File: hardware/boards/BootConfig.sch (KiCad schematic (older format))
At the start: 6 parts, among them SW1 SW_DIP_x03, U1 ECP5UM5G-381caBGA, U5 128MiB

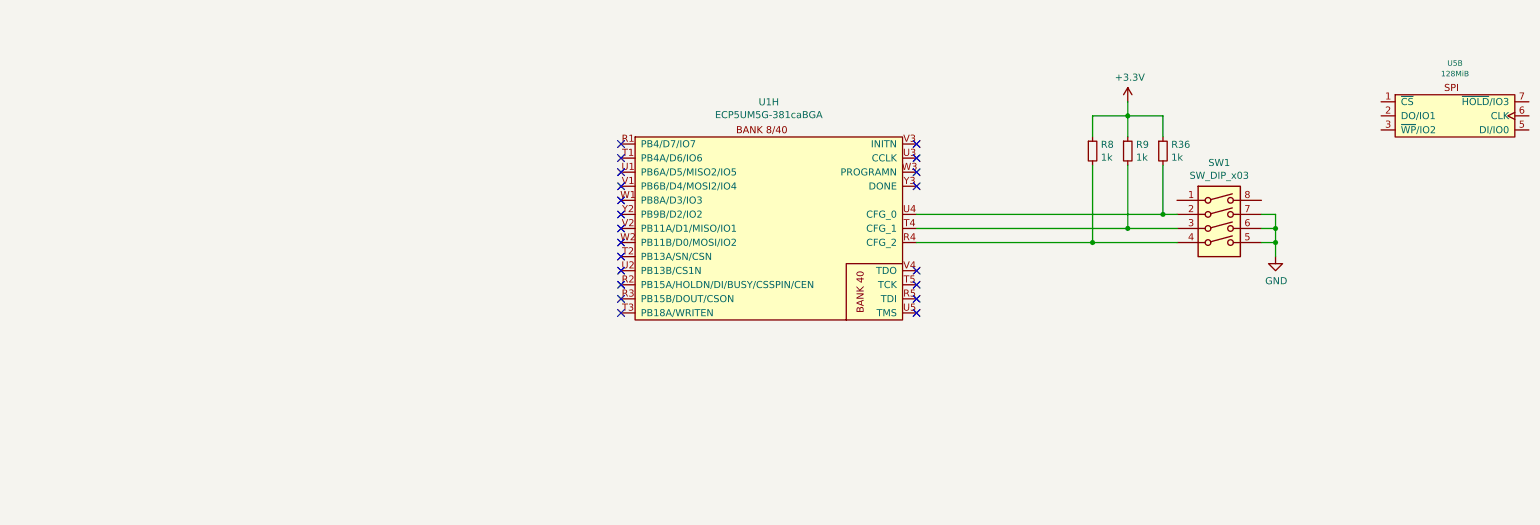
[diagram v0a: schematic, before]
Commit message: Added the JTAG header and some misc cleanup
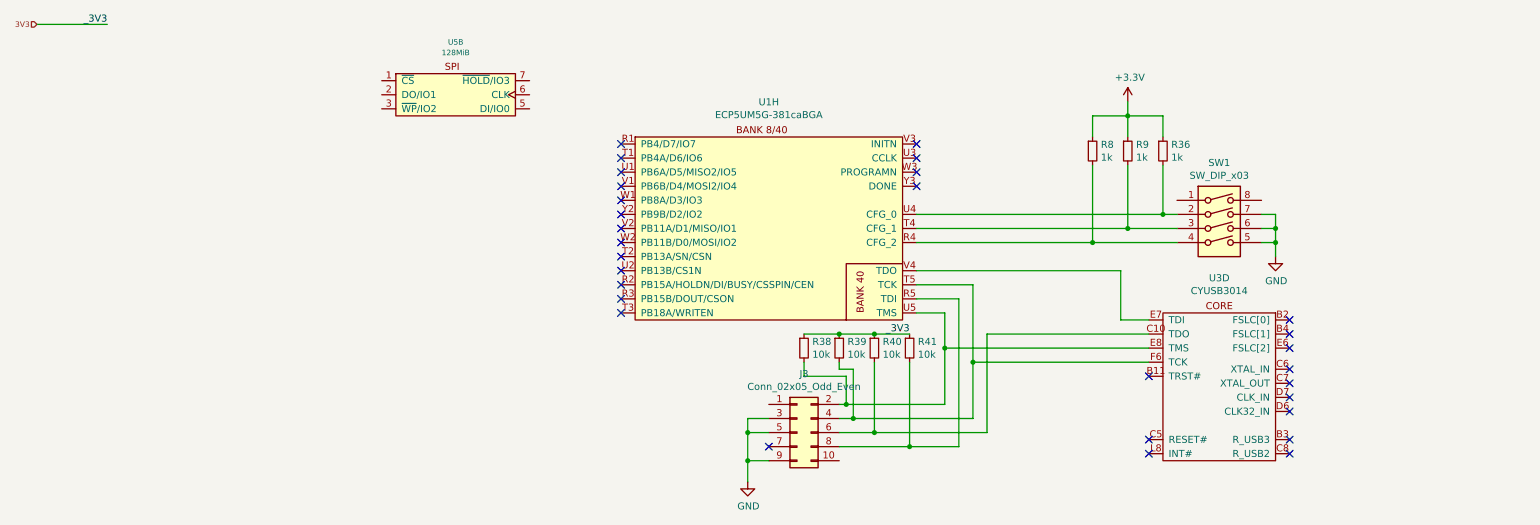
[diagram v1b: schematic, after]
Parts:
- added J3: Conn_02x05_Odd_Even, lethalbit-connectors:FTSH-105-01-L-DV-K-TR, symbol Connector_Generic:Conn_02x05_Odd_Even
- added R38, R39, R40, R41: 10k, Resistor_SMD:R_0603_1608Metric, symbol Device:R_Small
- added U3: CYUSB3014, lethalbit:BGA-121_11x11_10.0x10.0mm, symbol lethalbit:CYUSB3014
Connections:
- net GND: now also J3.3 (Pin_3), J3.5 (Pin_5), J3.9 (Pin_9)
- net at U1.R5 (TDI): now also J3.8 (Pin_8), R41.2
- net at U1.T5 (TCK): now also J3.4 (Pin_4), R39.2, U3.F6 (TCK)
- net at U1.U5 (TMS): now also J3.2 (Pin_2), R38.2, U3.E8 (TMS)
- net at U1.V4 (TDO): now also U3.E7 (TDI)
- new net: J3.6 (Pin_6), R40.2, U3.C10 (TDO)
- new net 3V3: R38.1, R39.1, R40.1, R41.1
- no-connect marks 21 -> 30
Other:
- moved on the sheet: U5B
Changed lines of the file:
@@
 NoConn ~ 4900 2550
 NoConn ~ 4900 2650
-NoConn ~ 7000 2650
-NoConn ~ 7000 2550
-NoConn ~ 7000 2450
-NoConn ~ 7000 2350
 NoConn ~ 7000 1750
 NoConn ~ 7000 1650
@@
 L lethalbit-memory:W25N01GVZEIG U5
 U 2 1 5F1F6855
-P 10800 1100
-F 0 "U5" H 10825 1324 39  0000 C CNN
-F 1 "128MiB" H 10825 1249 39  0000 C CNN
-F 2 "lethalbit-memory:WSON-8-1EP-6.0x8.0mm" H 10800 1250 39  0001 C CNN
-F 3 "https://www.winbond.com/resource-files/w25n01gv%20revl%20050918%20unsecured.pdf" H 10800 1250 39  0001 C CNN
-F 4 "Winbond" H 10800 1100 50  0001 C CNN "MFR"
-F 5 "W25N01GVZEIG TR" H 10800 1100 50  0001 C CNN "MPN"
-	2    10800 1100
-	1    0    0    -1
-$EndComp
+P 3700 950
+F 0 "U5" H 3725 1174 39  0000 C CNN
+F 1 "128MiB" H 3725 1099 39  0000 C CNN
+F 2 "lethalbit-memory:WSON-8-1EP-6.0x8.0mm" H 3700 1100 39  0001 C CNN
+F 3 "https://www.winbond.com/resource-files/w25n01gv%20revl%20050918%20unsecured.pdf" H 3700 1100 39  0001 C CNN
+F 4 "Winbond" H 3700 950 50  0001 C CNN "MFR"
+F 5 "W25N01GVZEIG TR" H 3700 950 50  0001 C CNN "MPN"
+	2    3700 950
+	1    0    0    -1
+$EndComp
+$Comp
+L Connector_Generic:Conn_02x05_Odd_Even J3
+U 1 1 5FC2DE7F
+P 6150 3500
+F 0 "J3" H 6200 3917 50  0000 C CNN
+F 1 "Conn_02x05_Odd_Even" H 6200 3826 50  0000 C CNN
+F 2 "lethalbit-connectors:FTSH-105-01-L-DV-K-TR" H 6150 3500 50  0001 C CNN
+F 3 "~" H 6150 3500 50  0001 C CNN
+F 4 "Samtec" H 6150 3500 50  0001 C CNN "MFR"
+F 5 "FTSH-105-01-L-DV-K-TR" H 6150 3500 50  0001 C CNN "MPN"
+	1    6150 3500
+	1    0    0    -1
+$EndComp
+NoConn ~ 5950 3600
+$Comp
+L power:GND #PWR0127
+U 1 1 5FC38CCB
+P 5800 3850
+F 0 "#PWR0127" H 5800 3600 50  0001 C CNN
+F 1 "GND" H 5805 3677 50  0000 C CNN
+F 2 "" H 5800 3850 50  0001 C CNN
+F 3 "" H 5800 3850 50  0001 C CNN
+	1    5800 3850
+	1    0    0    -1
+$EndComp
+Wire Wire Line
+	5800 3850 5800 3700
+Wire Wire Line
+	5800 3400 5950 3400
+Wire Wire Line
+	5950 3500 5800 3500
+Connection ~ 5800 3500
+Wire Wire Line
+	5800 3500 5800 3400
+Wire Wire Line
+	5950 3700 5800 3700
+Connection ~ 5800 3700
+Wire Wire Line
+	5800 3700 5800 3500
+NoConn ~ 9650 2700
+NoConn ~ 9650 2800
+NoConn ~ 9650 2900
+NoConn ~ 9650 3050
+NoConn ~ 9650 3150
+NoConn ~ 9650 3250
+NoConn ~ 9650 3350
+NoConn ~ 9650 3550
+NoConn ~ 9650 3650
+NoConn ~ 8650 3650
+NoConn ~ 8650 3550
+NoConn ~ 8650 3100
+$Comp
+L lethalbit:CYUSB3014 U?
+U 4 1 5FC667B5
+P 9150 3200
+AR Path="/5F2CAFD2/5FC667B5" Ref="U?"  Part="4"
+AR Path="/5EF66251/5FC667B5" Ref="U3"  Part="4"
+F 0 "U3" H 9150 3998 50  0000 C CNN
+F 1 "CYUSB3014" H 9150 3907 50  0000 C CNN
+F 2 "lethalbit:BGA-121_11x11_10.0x10.0mm" H 9150 3900 50  0001 C CNN
+F 3 "https://www.cypress.com/file/140296/download" H 9150 3900 50  0001 C CNN
+F 4 "Cypress" H 9150 3200 50  0001 C CNN "MFR"
+F 5 " CYUSB3014-BZXI" H 9150 3200 50  0001 C CNN "MPN"
+F 6 "428-3130-ND" H 9150 3200 50  0001 C CNN "DIGIKEY_PN"
+	4    9150 3200
+	-1   0    0    -1
+$EndComp
+Wire Wire Line
+	6450 3600 6950 3600
+Wire Wire Line
+	7300 3600 7300 2550
+Wire Wire Line
+	7300 2550 7000 2550
+Wire Wire Line
+	6450 3300 6500 3300
+Wire Wire Line
+	7200 3300 7200 2900
+Wire Wire Line
+	7200 2650 7000 2650
+Wire Wire Line
+	7000 2350 8450 2350
+Wire Wire Line
+	8450 2350 8450 2700
+Wire Wire Line
+	8450 2700 8650 2700
+Wire Wire Line
+	6450 3500 6700 3500
+Wire Wire Line
+	7500 3500 7500 2800
+Wire Wire Line
+	7500 2800 8650 2800
+Wire Wire Line
+	6450 3400 6550 3400
+Wire Wire Line
+	7400 3400 7400 3000
+Wire Wire Line
+	7400 2450 7000 2450
+Wire Wire Line
+	7200 2900 8650 2900
+Connection ~ 7200 2900
+Wire Wire Line
+	7200 2900 7200 2650
+Wire Wire Line
+	7400 3000 8650 3000
+Connection ~ 7400 3000
+Wire Wire Line
+	7400 3000 7400 2450
+Text HLabel 750  600  0    39   Input ~ 0
+3V3
+Wire Wire Line
+	750  600  1250 600
+Text Label 1250 600  2    50   ~ 0
+_3V3
+$Comp
+L Device:R_Small R?
+U 1 1 5FDE1FC1
+P 6200 2900
+AR Path="/5EDF9F51/5FDE1FC1" Ref="R?"  Part="1"
+AR Path="/5EF66251/5FDE1FC1" Ref="R38"  Part="1"
+F 0 "R38" H 6259 2946 50  0000 L CNN
+F 1 "10k" H 6259 2855 50  0000 L CNN
+F 2 "Resistor_SMD:R_0603_1608Metric" H 6200 2900 50  0001 C CNN
+F 3 "~" H 6200 2900 50  0001 C CNN
+F 4 "Vishay Dale" H 6200 2900 50  0001 C CNN "MFR"
+F 5 "CRCW060310K0FKEA" H 6200 2900 50  0001 C CNN "MPN"
+	1    6200 2900
+	1    0    0    -1
+$EndComp
+$Comp
+L Device:R_Small R?
+U 1 1 5FDE1FC9
+P 6450 2900
+AR Path="/5EDF9F51/5FDE1FC9" Ref="R?"  Part="1"
+AR Path="/5EF66251/5FDE1FC9" Ref="R39"  Part="1"
+F 0 "R39" H 6509 2946 50  0000 L CNN
+F 1 "10k" H 6509 2855 50  0000 L CNN
+F 2 "Resistor_SMD:R_0603_1608Metric" H 6450 2900 50  0001 C CNN
+F 3 "~" H 6450 2900 50  0001 C CNN
+F 4 "Vishay Dale" H 6450 2900 50  0001 C CNN "MFR"
+F 5 "CRCW060310K0FKEA" H 6450 2900 50  0001 C CNN "MPN"
+	1    6450 2900
+	1    0    0    -1
+$EndComp
+$Comp
+L Device:R_Small R?
+U 1 1 5FDE1FD1
+P 6700 2900
+AR Path="/5EDF9F51/5FDE1FD1" Ref="R?"  Part="1"
+AR Path="/5EF66251/5FDE1FD1" Ref="R40"  Part="1"
+F 0 "R40" H 6759 2946 50  0000 L CNN
+F 1 "10k" H 6759 2855 50  0000 L CNN
+F 2 "Resistor_SMD:R_0603_1608Metric" H 6700 2900 50  0001 C CNN
+F 3 "~" H 6700 2900 50  0001 C CNN
+F 4 "Vishay Dale" H 6700 2900 50  0001 C CNN "MFR"
+F 5 "CRCW060310K0FKEA" H 6700 2900 50  0001 C CNN "MPN"
+	1    6700 2900
+	1    0    0    -1
+$EndComp
+Text Label 6950 2800 2    50   ~ 0
+_3V3
+Connection ~ 6700 2800
+Connection ~ 6450 2800
+Wire Wire Line
+	6450 2800 6700 2800
+Wire Wire Line
+	6200 2800 6450 2800
+Wire Wire Line
+	6700 2800 6950 2800
+$Comp
+L Device:R_Small R?
+U 1 1 5FDE1FD9
+P 6950 2900
+AR Path="/5EDF9F51/5FDE1FD9" Ref="R?"  Part="1"
+AR Path="/5EF66251/5FDE1FD9" Ref="R41"  Part="1"
+F 0 "R41" H 7009 2946 50  0000 L CNN
+F 1 "10k" H 7009 2855 50  0000 L CNN
+F 2 "Resistor_SMD:R_0603_1608Metric" H 6950 2900 50  0001 C CNN
+F 3 "~" H 6950 2900 50  0001 C CNN
+F 4 "Vishay Dale" H 6950 2900 50  0001 C CNN "MFR"
+F 5 "CRCW060310K0FKEA" H 6950 2900 50  0001 C CNN "MPN"
+	1    6950 2900
+	1    0    0    -1
+$EndComp
+Wire Wire Line
+	6200 3000 6200 3100
+Wire Wire Line
+	6200 3100 6500 3100
+Wire Wire Line
+	6500 3100 6500 3300
+Connection ~ 6500 3300
+Wire Wire Line
+	6500 3300 7200 3300
+Wire Wire Line
+	6450 3000 6450 3050
+Wire Wire Line
+	6450 3050 6550 3050
+Wire Wire Line
+	6550 3050 6550 3400
+Connection ~ 6550 3400
+Wire Wire Line
+	6550 3400 7400 3400
+Wire Wire Line
+	6700 3000 6700 3500
+Connection ~ 6700 3500
+Wire Wire Line
+	6700 3500 7500 3500
+Wire Wire Line
+	6950 3000 6950 3600
+Connection ~ 6950 3600
+Wire Wire Line
+	6950 3600 7300 3600
 $EndSCHEMATC

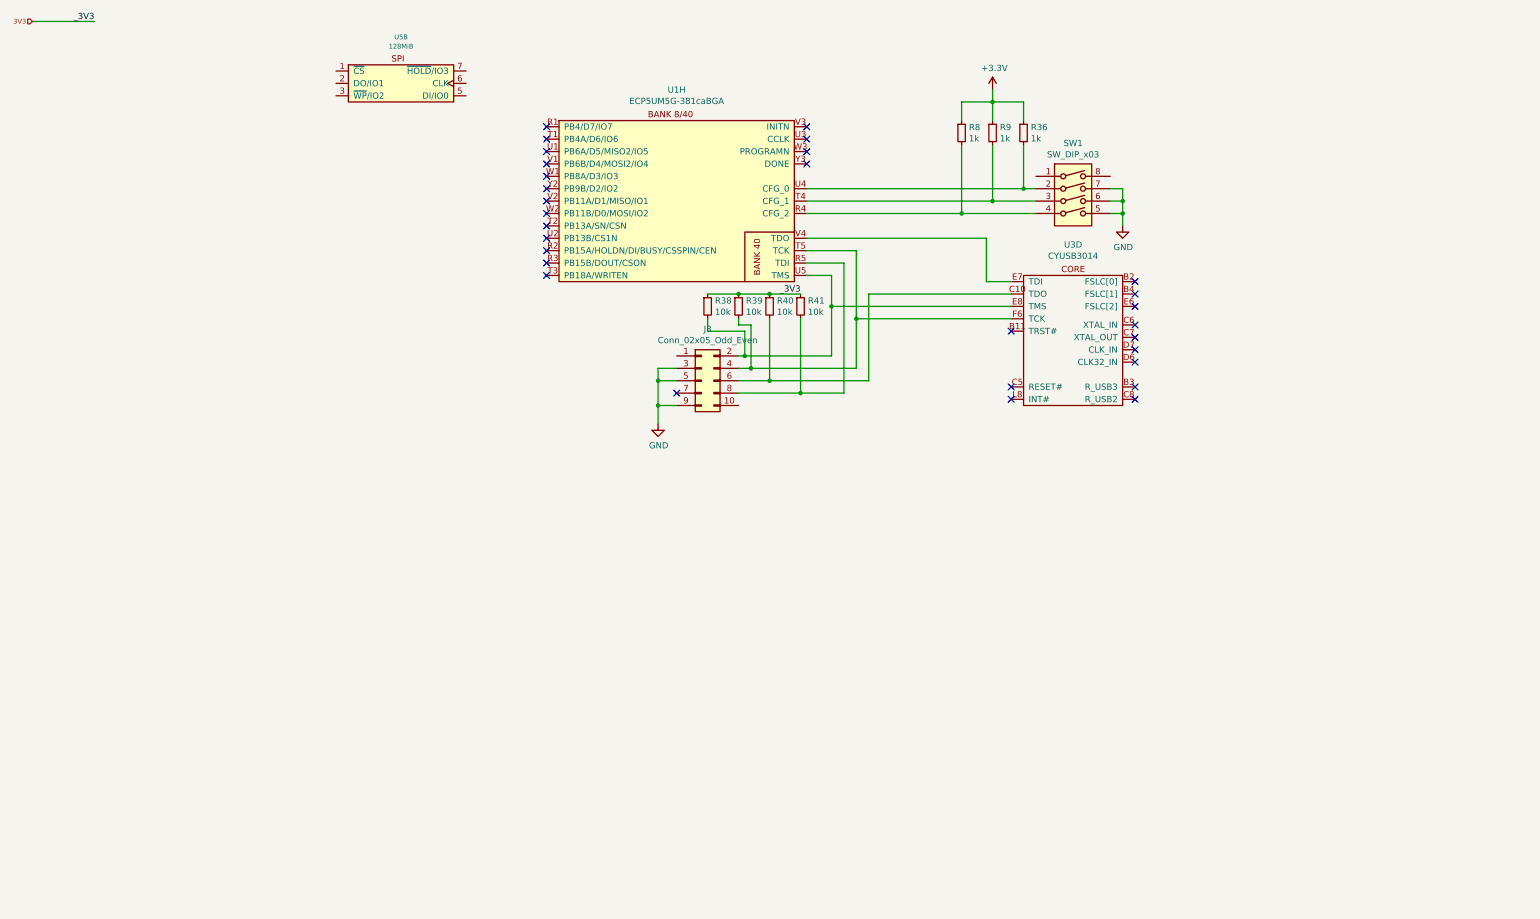
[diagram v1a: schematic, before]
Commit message: Added a secondary SPI flash for the USB PHY Firmware. Yes it's overkill but it'll be fine. I'll use it to like, store configuration data or something
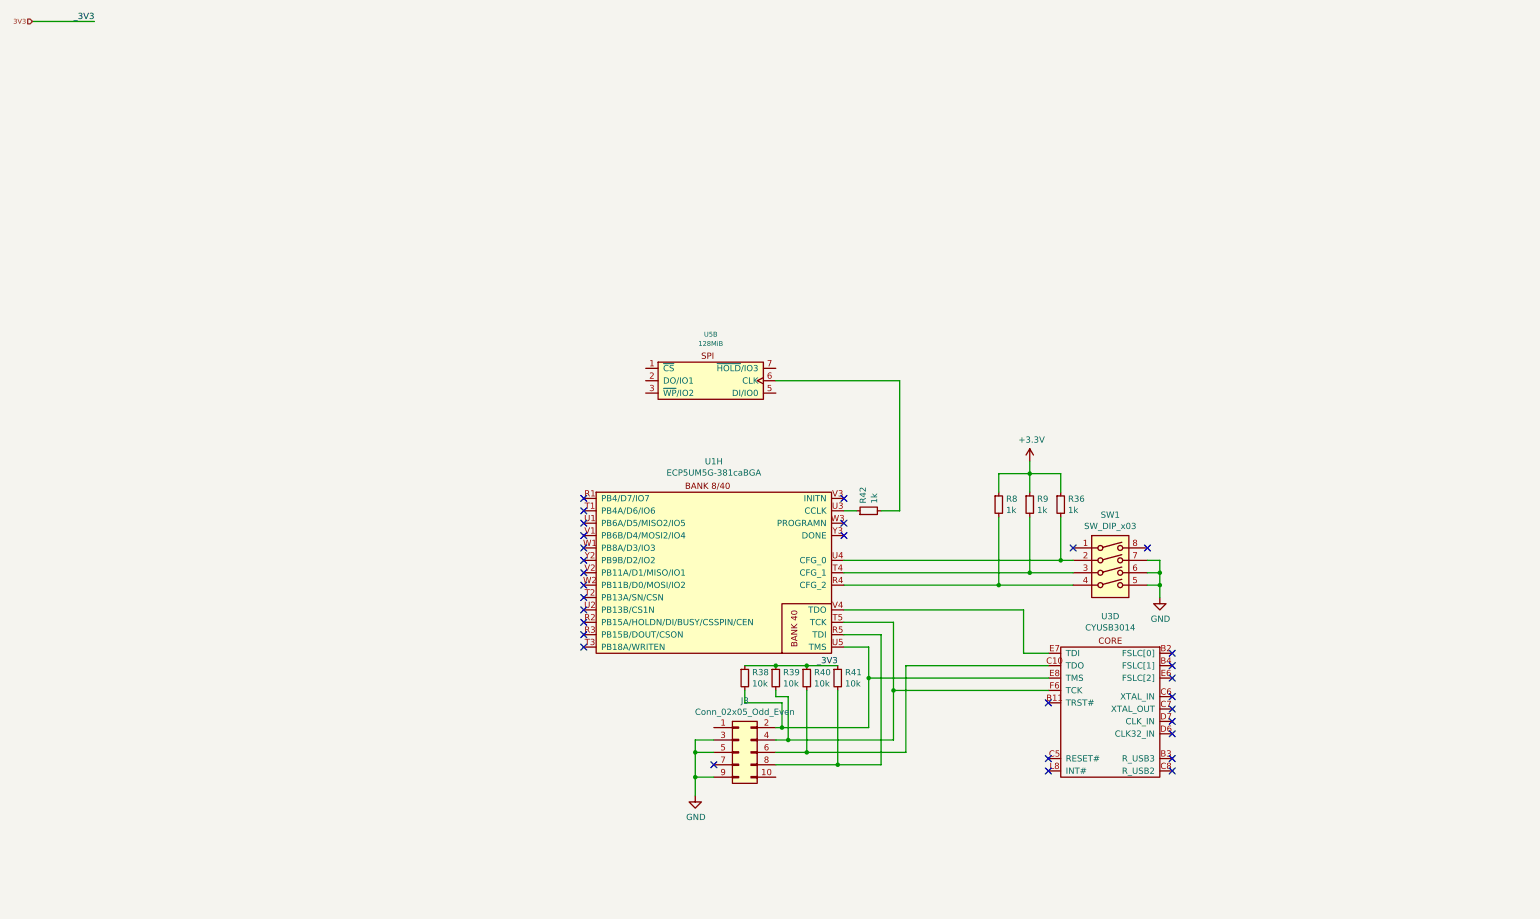
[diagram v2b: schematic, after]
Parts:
- added R42: 1k, Resistor_SMD:R_0603_1608Metric, symbol Device:R_Small
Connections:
- net at U5.6 (CLK): now also R42.2
- net at U1.U3 (CCLK): now also R42.1
- no-connect marks 30 -> 31
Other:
- moved on the sheet: J3, R36, R38, R39, R40, R41, R8, R9, SW1, U1H, U3D, U5B

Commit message: Added a bunch of stuff having to do with JTAG and the FPGA flash / bring up
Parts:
- added D?: PNK, LED_SMD:LED_0603_1608Metric, symbol Device:LED
- added D?: RED, LED_SMD:LED_0603_1608Metric, symbol Device:LED
- added D?: BLU, LED_SMD:LED_0603_1608Metric, symbol Device:LED
- added Q?: Q_NMOS_GSD, Package_TO_SOT_SMD:SOT-23, symbol Device:Q_NMOS_GSD
- added R? (x8): 10k, Resistor_SMD:R_0603_1608Metric, symbol Device:R_Small
- added R?: 4k7, Resistor_SMD:R_0603_1608Metric, symbol Device:R_Small
- added SW?: RESET, symbol Switch:SW_Push
- R42: value 1k -> 50; MPN CRCW06031K00FKEAHP -> CRCW060350R0FKEA
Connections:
- net +3V3: now also R?.1
- net 3V3: now also J3.1 (Pin_1), R?.1, R?.1, R?.1, R?.1, R?.1, R?.1, R?.1
- net GND: now also Q?.2 (S), SW?.2
- net at U5.1 (~CS): now also U1.R2 (PB15A/HOLDN/DI/BUSY/CSSPIN/CEN)
- net at U5.2 (DO/IO1): now also U1.W2 (PB11B/D0/MOSI/IO2), R?.2
- net at U5.3 (~WP~/IO2): now also U1.Y2 (PB9B/D2/IO2), R?.2
- net at U5.5 (DI/IO0): now also U1.V2 (PB11A/D1/MISO/IO1), R?.2
- net at U5.6 (CLK): now also R42.1; no longer R42.2
- net at U5.7 (~HOLD~/IO3): now also U1.W1 (PB8A/D3/IO3), R?.2
- net at U1.U3 (CCLK): now also R42.2; no longer R42.1
- net at U1.V3 (INITN): now also D?.1 (K)
- net at U1.W3 (PROGRAMN): now also J3.10 (Pin_10), U3.B11 (TRST#), D?.1 (K), R?.2, SW?.1
- net at U1.Y3 (DONE): now also R?.2
- new net: D?.2 (A), R?.2 (x3)
- new net: Q?.1 (G), R?.1
- new net: D?.1 (K), Q?.3 (D)
- no-connect marks 31 -> 22
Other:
- note added: "CFG[0..2] should be\n0 1 0 for SPI master."
- note added: "I *think* this is correct?"
- note added: "SWD/JTAG Pinout:\n01 - 3v3\n02 - TMS\n03 - GND\n04 - TCK\n05 - GND\n06 - TDO\n07 - NC\n08 - TDI\n09 - GND\n10 - ~PROGRAM/RESET"
- note added: "This should just be replaced with the proper\npull-ups/downs to statically configure,\nbut for rev 0 lets let it be configurable."
- moved on the sheet: R36, R42, R8, R9, SW1
